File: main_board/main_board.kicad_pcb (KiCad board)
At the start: 2 copper layers, 145 x 87 mm, 132 parts, among them J1 stepper 0, J10 24VDCout5, J11 5VDCout0, J12 5VDCout1, J13 5VDCout2, J14 5VDCout3, J15 5VDCout4, J16 5VDCout5, J17 temp 0, J18 temp 1, J19 I2C, J2 stepper 1, J20 I2C, J21 I2C, J22 I2C, J23 hall 0, J24 weight 0, J25 light 0, J26 24VDC_in, J27 24VDC to 5VDC step down, J28 24VDC, J29 24VDC, J3 stepper 2, J30 24VDC, J31 5VDC, J32 5VDC, J33 5VDC, J34 hall 1, J35 reflective 0, J36 24VDC, J37 24VDC, J38 24VDC, J39 5VDC, J4 stepper 3, J40 5VDC, J41 5VDC, J42 encoder, J5 24VDCout0, J6 24VDCout1, J7 24VDCout2, J8 24VDCout3, J9 24VDCout4, Q1 Q_NMOS_GDS, Q10 BS170, Q11 BS170, Q12 BS170, Q2 Q_NMOS_GDS, Q3 Q_NMOS_GDS, Q4 Q_NMOS_GDS, Q5 Q_NMOS_GDS, Q6 Q_NMOS_GDS, Q7 BS170, Q8 BS170, Q9 BS170, U1 ESP32-DEVKITC-32D, U2 PCA9685PW

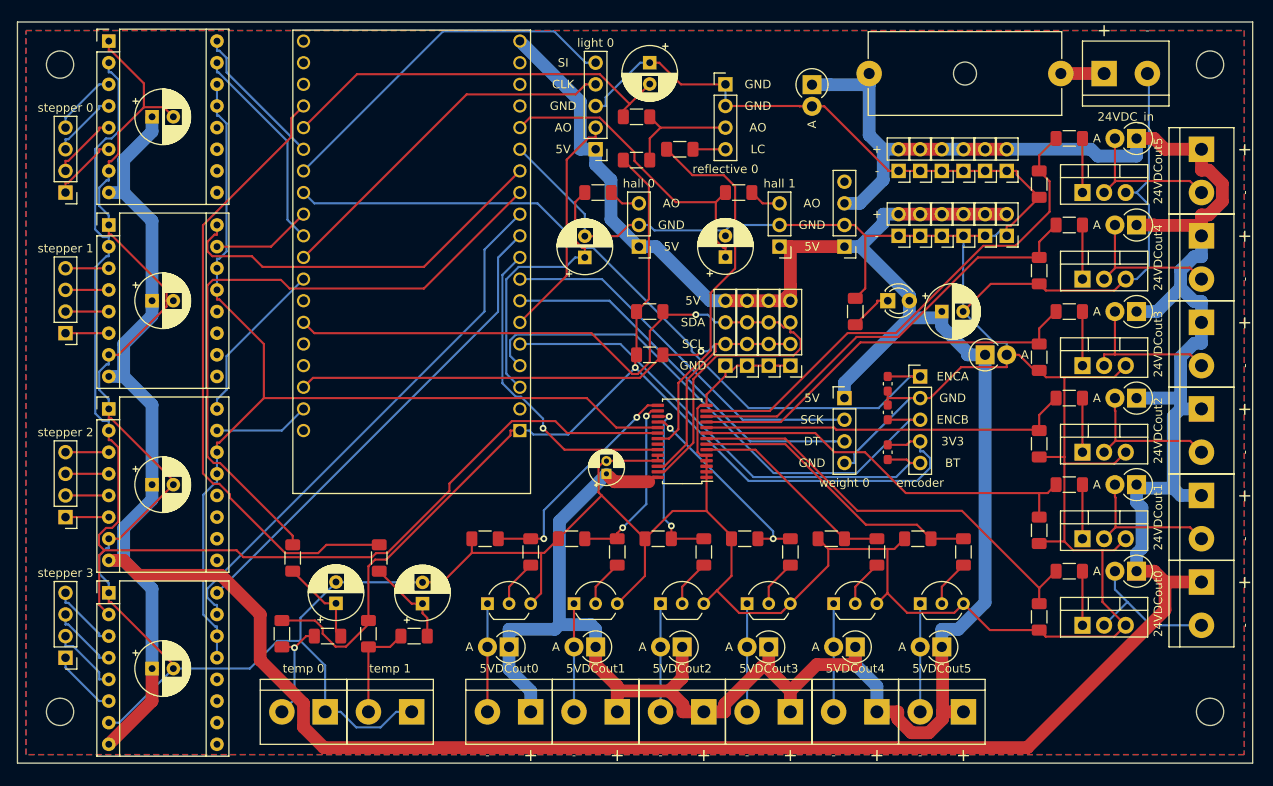
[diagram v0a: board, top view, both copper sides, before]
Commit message: part numbers added
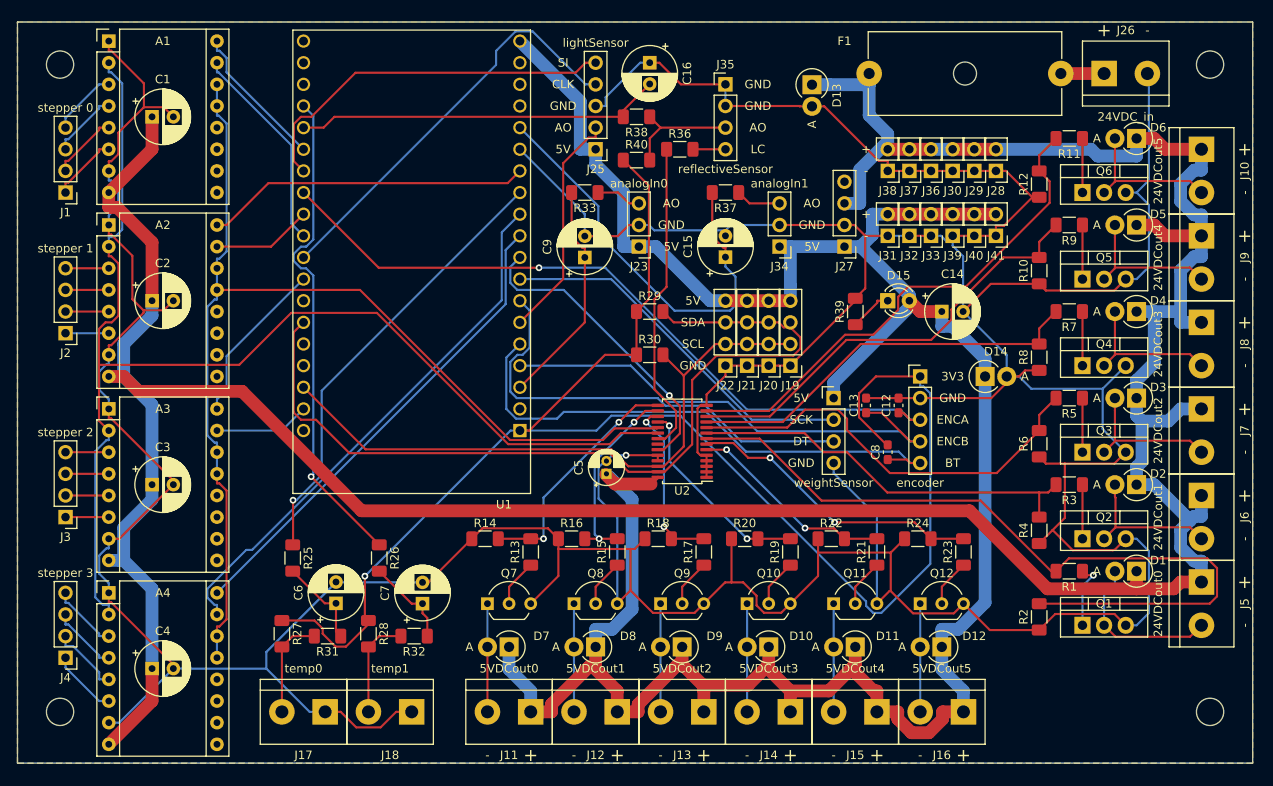
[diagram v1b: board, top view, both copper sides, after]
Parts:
- J17: value temp 0 -> temp0
- J18: value temp 1 -> temp1
- J23: value hall 0 -> analogIn0
- J24: value weight 0 -> weightSensor
- J25: value light 0 -> lightSensor
- J34: value hall 1 -> analogIn1
- J35: value reflective 0 -> reflectiveSensor
- moved C12 2.84 mm to (138.4, 58.0)
- moved C13 2.67 mm to (134.6, 58.0)
- moved D14 2.54 mm to (148.6, 54.6)
- moved R33 1.55 mm to (101.6, 33.0)
- moved R37 1.55 mm to (118.1, 33.0)
- moved J24 1.27 mm to (130.8, 57.1)
- moved J29 1.27 mm to (147.3, 30.5)
- moved J30 1.27 mm to (144.8, 30.5)
- moved J31 1.27 mm to (137.2, 38.1)
- moved J32 1.27 mm to (139.7, 38.1)
- moved J37 1.27 mm to (139.7, 30.5)
- moved J38 1.27 mm to (137.2, 30.5)
- moved J39 1.27 mm to (144.8, 38.1)
- moved J40 1.27 mm to (147.3, 38.1)
- moved J28 1.27 mm to (149.9, 30.5)
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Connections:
- C12 pad 1: GND -> enca
- C12 pad 2: enca -> GND
- J42 pad 1: enca -> +3V3
- J42 pad 3: encb -> enca
- J42 pad 4: +3V3 -> encb
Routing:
- net +3V3: track 136.2 -> 185.4 mm
- net 24VDC_output0: track 50.9 -> 92.0 mm
- net GND: track 655.5 -> 683.2 mm, vias 0 -> 1
- net Net-(R25-Pad1): track 77.1 -> 52.6 mm, vias 0 -> 1
- net Net-(R26-Pad1): track 73.2 -> 58.0 mm, vias 0 -> 1
- net hallmeasure1: track 36.9 -> 51.0 mm
- net +24V: track 399.1 -> 388.3 mm
- net stepperON: track 122.7 -> 130.7 mm
- net DT: track 44.9 -> 52.8 mm
- net DIR1: track 45.8 -> 38.2 mm
- net LEDcon0: track 44.0 -> 37.0 mm
- net 24VDC_output2: track 43.8 -> 50.5 mm
- net encb: track 65.0 -> 58.4 mm
- net SDA: track 96.7 -> 103.1 mm, vias 1 -> 0
- net CLK: track 42.7 -> 48.8 mm
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- added copper zone on B.Cu, net (none)
- removed copper zone on B.Cu, net GND

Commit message: GND zones added
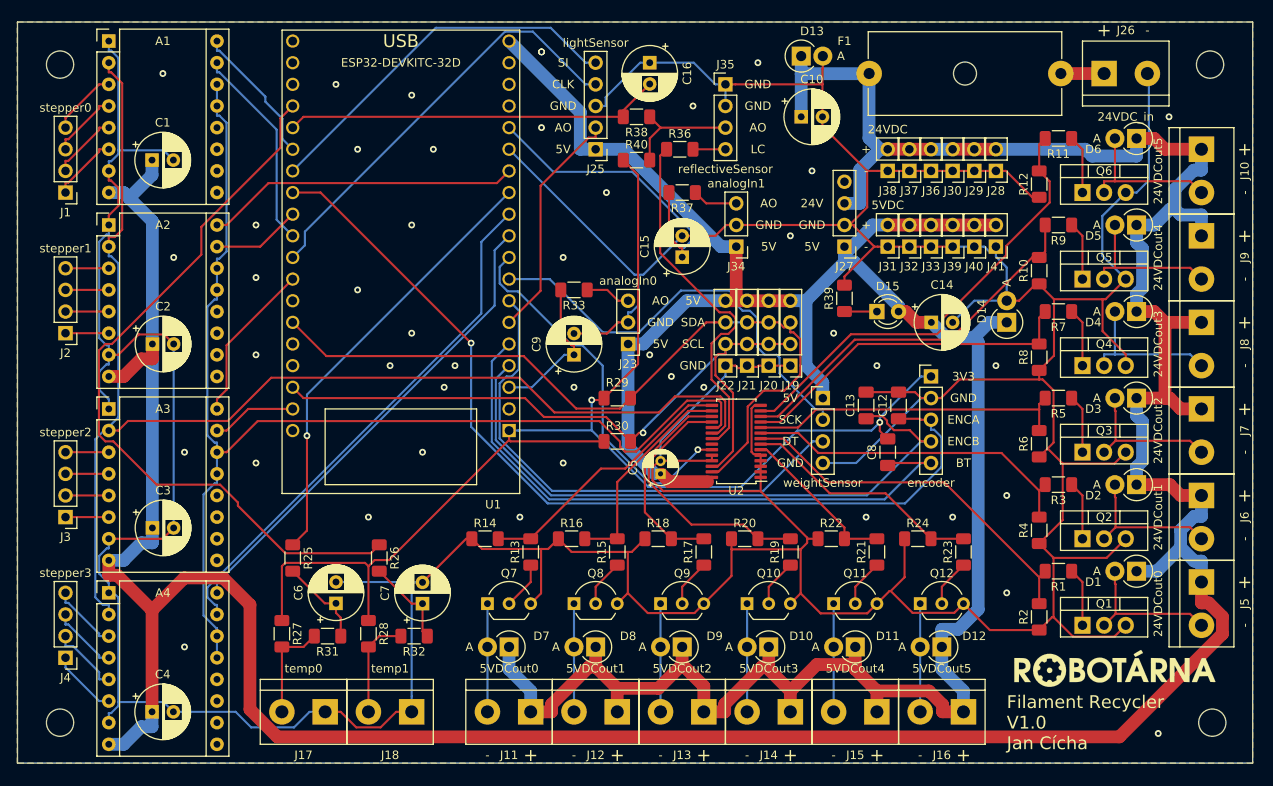
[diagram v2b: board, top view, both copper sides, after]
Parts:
- added C10: 100uF, Capacitor_THT:CP_Radial_D6.3mm_P2.50mm, F.Cu at (127.0, 24.1)
- added G***: LOGO, main_board:robotarna_logo, F.Cu at (163.8, 88.9)
- C12, C13, C8: footprint Capacitor_SMD:C_0603_1608Metric_Pad1.08x0.95mm_HandSolder -> Capacitor_SMD:C_1206_3216Metric_Pad1.33x1.80mm_HandSolder
- J1: value stepper 0 -> stepper0
- J2: value stepper 1 -> stepper1
- J3: value stepper 2 -> stepper2
- J4: value stepper 3 -> stepper3
- moved C9 11.5 mm to (100.3, 52.1)
- moved J23 11.5 mm to (106.7, 50.8)
- moved R33 11.5 mm to (100.3, 44.5)
- moved R29 10.9 mm to (105.4, 57.1)
- moved R30 10.9 mm to (105.4, 62.2)
- moved D14 6.84 mm to (151.1, 48.3), turned to 90 degrees
- moved C5 6.35 mm to (110.5, 66.0)
- moved U2 6.35 mm to (119.4, 62.2)
- moved C2 5.08 mm to (50.8, 50.8)
- moved C3 5.08 mm to (50.8, 72.4)
- moved C1 5.08 mm to (50.8, 29.2)
- moved C15 5.08 mm to (113.0, 40.6)
- moved C4 5.08 mm to (50.8, 94.0)
- moved J34 5.08 mm to (119.4, 39.4)
- moved R37 5.08 mm to (113.0, 33.0)
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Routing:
- net 24VDC_output0: track 92.0 -> 43.5 mm
- net +3V3: track 185.4 -> 153.9 mm, vias 1 -> 2
- net Net-(R26-Pad1): track 58.0 -> 87.8 mm, vias 1 -> 0
- net +24V: track 388.3 -> 415.0 mm
- net GND: track 683.2 -> 708.7 mm, vias 1 -> 43
- net enca: track 86.3 -> 108.9 mm
- net encb: track 58.4 -> 74.9 mm
- net 24VDC_output2: track 50.5 -> 37.7 mm
- net hallmeasure1: track 51.0 -> 38.5 mm
- net SDA: track 103.1 -> 91.5 mm
- net stepperON: track 130.7 -> 140.3 mm
- net button: track 64.1 -> 73.7 mm
- net hallmeasure0: track 26.8 -> 17.6 mm
- net SCL: track 75.3 -> 84.3 mm, vias 0 -> 1
- net OE: track 35.9 -> 44.7 mm
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- added copper zone on B.Cu, net GND
- removed copper zone on B.Cu, net (none)
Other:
- board text added: "24V"
- board text added: "Filament Recycler V1.0 Jan Cícha"
- board text added: "USB"

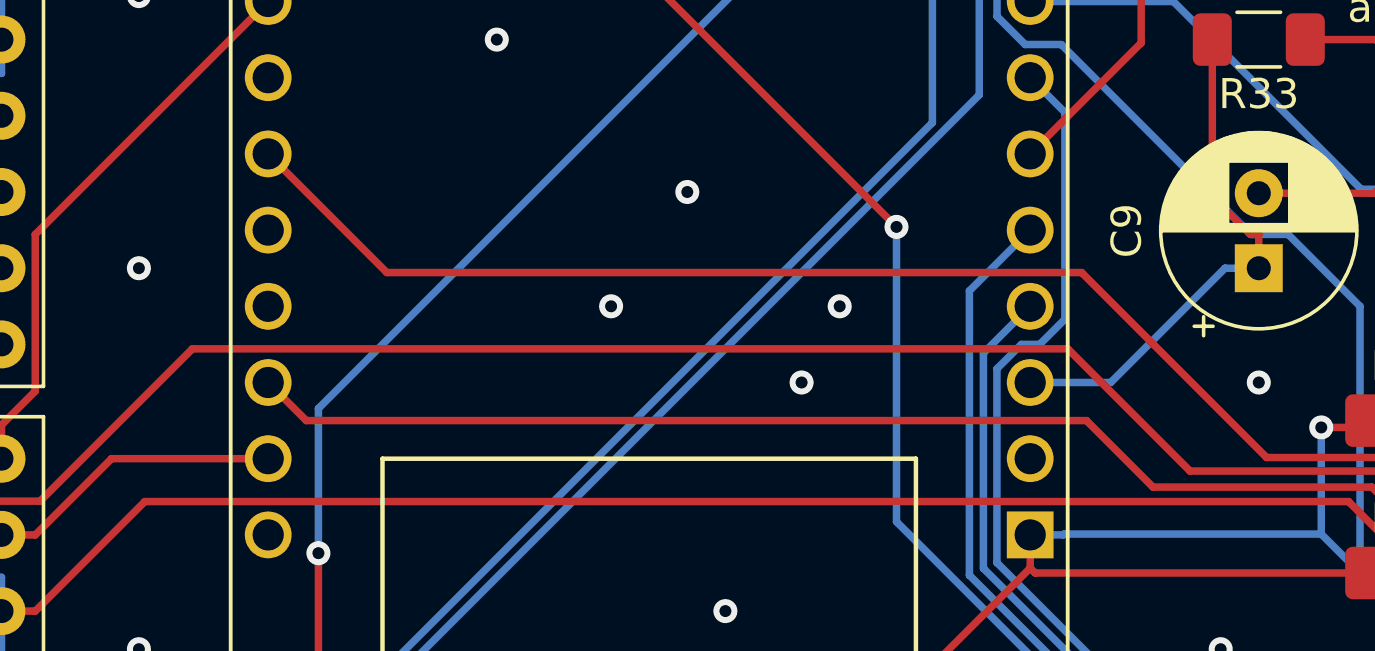
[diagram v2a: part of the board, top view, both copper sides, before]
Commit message: GND zone update
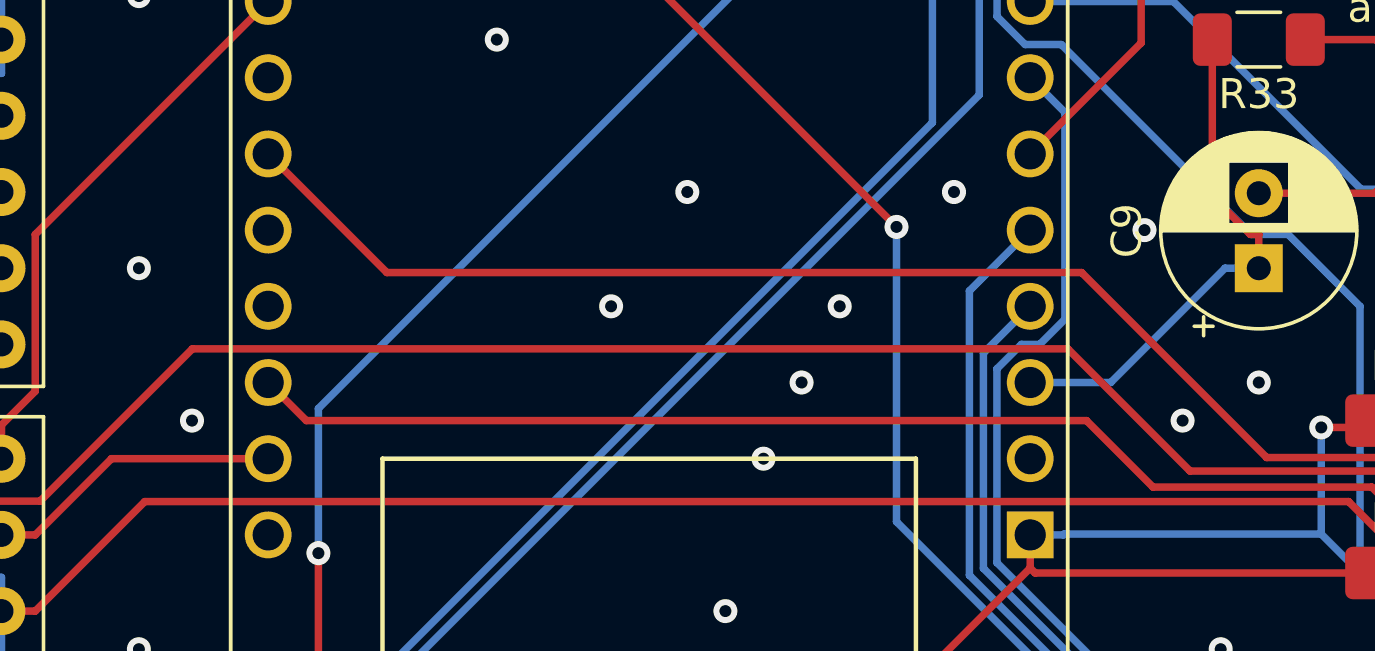
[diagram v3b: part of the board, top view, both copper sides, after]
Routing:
- net GND: vias 43 -> 48
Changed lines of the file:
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@@
     (thickness 1.6)
     (drawings 71)
-    (tracks 1045)
+    (tracks 1050)
     (zones 0)
     (modules 134)
@@
   (via (at 96.52 16.51) (size 0.8) (drill 0.4) (layers F.Cu B.Cu) (net 4))
   (via (at 109.22 52.07) (size 0.8) (drill 0.4) (layers F.Cu B.Cu) (net 4))
+  (via (at 83.82 58.42) (size 0.8) (drill 0.4) (layers F.Cu B.Cu) (net 4))
+  (via (at 97.79 57.15) (size 0.8) (drill 0.4) (layers F.Cu B.Cu) (net 4))
+  (via (at 64.77 57.15) (size 0.8) (drill 0.4) (layers F.Cu B.Cu) (net 4))
+  (via (at 96.52 50.8) (size 0.8) (drill 0.4) (layers F.Cu B.Cu) (net 4))
+  (via (at 90.17 49.53) (size 0.8) (drill 0.4) (layers F.Cu B.Cu) (net 4))
   (segment (start 58.42 63.5) (end 59.5453 63.5) (width 0.25) (layer F.Cu) (net 5))
   (segment (start 59.5453 63.5) (end 63.196 59.8493) (width 0.25) (layer F.Cu) (net 5))

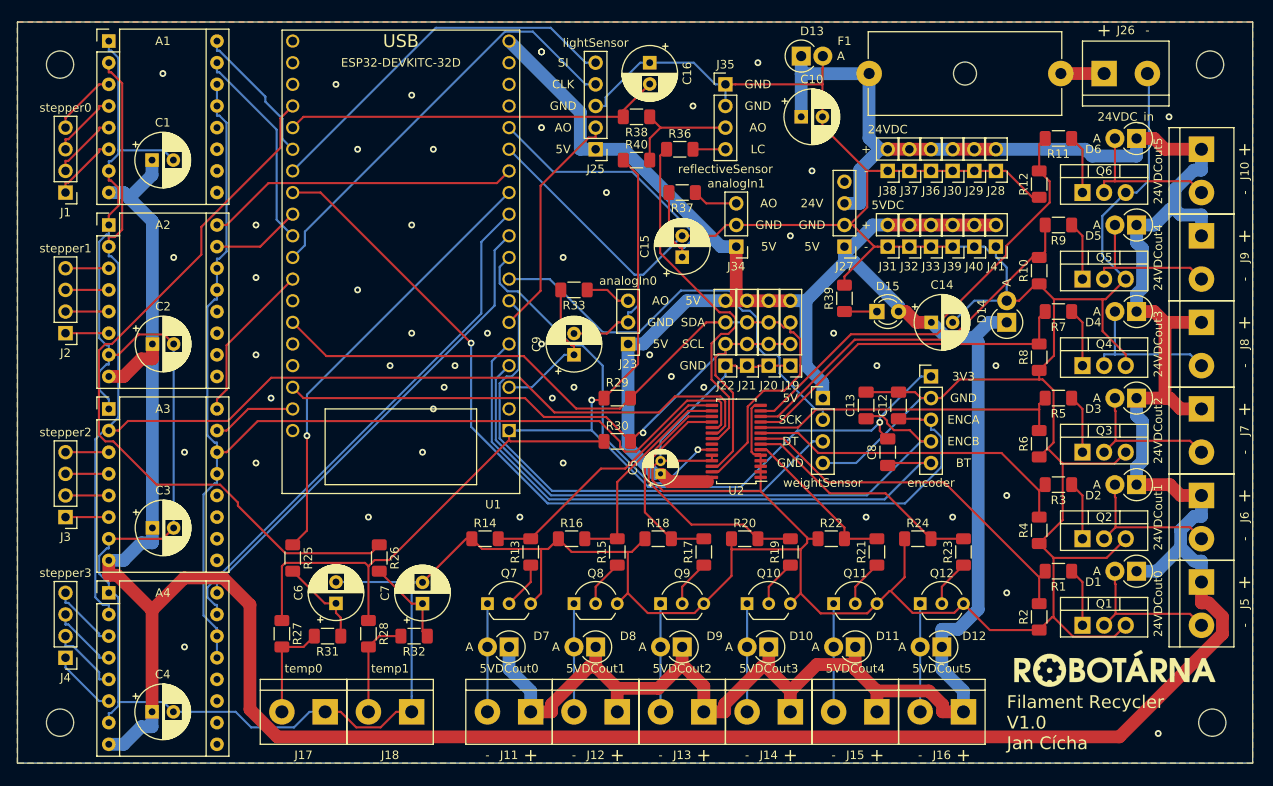
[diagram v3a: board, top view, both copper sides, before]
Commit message: ADC 2 unused
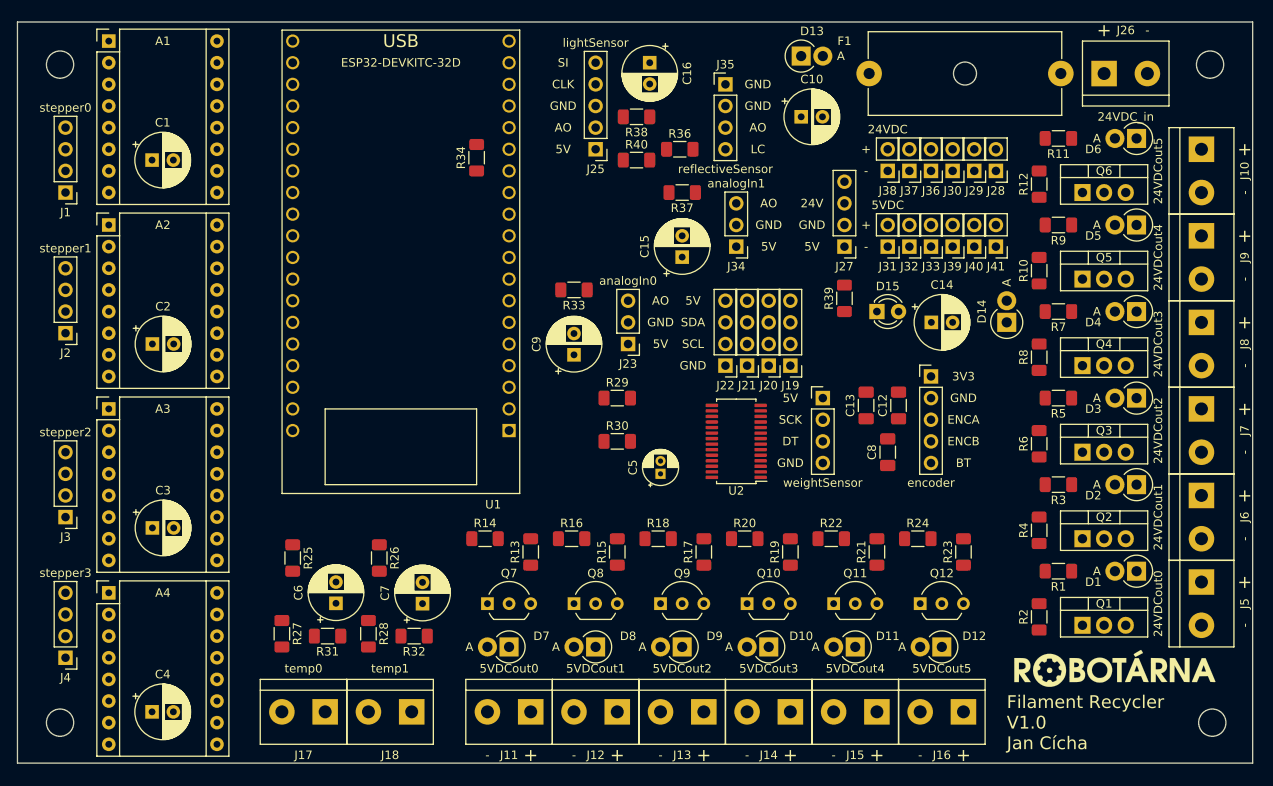
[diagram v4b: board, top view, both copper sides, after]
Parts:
- added R34: 10k, Resistor_SMD:R_1206_3216Metric_Pad1.30x1.75mm_HandSolder, F.Cu at (88.9, 28.9)
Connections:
- J17 pad 1: GND -> Net-(J17-Pad1)
- J17 pad 2: Net-(J17-Pad2) -> GND
- J18 pad 1: GND -> Net-(J18-Pad1)
- J18 pad 2: Net-(J18-Pad2) -> GND
- J35 pad 2: GND -> +5V
- R27 pad 2: Net-(J17-Pad2) -> Net-(J17-Pad1)
- R28 pad 2: Net-(J18-Pad2) -> Net-(J18-Pad1)
- R31 pad 2: Net-(J17-Pad2) -> Net-(J17-Pad1)
- R32 pad 2: Net-(J18-Pad2) -> Net-(J18-Pad1)
- U1 pad 32: SI -> reflectivesensor0
- U1 pad 34: reflectivesensor0 -> SI
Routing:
- net GND: track 708.7 -> 0.00 mm, vias 48 -> 0
- net +24V: track 415.0 -> 0.00 mm
- net +5V: track 297.4 -> 0.00 mm
- net +3V3: track 153.9 -> 0.00 mm, vias 2 -> 0
- net stepperErr: track 152.5 -> 0.00 mm
- net stepperON: track 140.3 -> 0.00 mm
- net enca: track 108.9 -> 0.00 mm, vias 1 -> 0
- net SDA: track 91.5 -> 0.00 mm
- net Net-(R26-Pad1): track 87.8 -> 0.00 mm
- net SCL: track 84.3 -> 0.00 mm, vias 1 -> 0
- net encb: track 74.9 -> 0.00 mm
- net button: track 73.7 -> 0.00 mm
- net STEP3: track 62.3 -> 0.00 mm
- net DT: track 60.8 -> 0.00 mm
- net DIR3: track 56.1 -> 0.00 mm
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- removed copper zone on B.Cu, net GND
- removed copper zone on F.Cu, net GND
